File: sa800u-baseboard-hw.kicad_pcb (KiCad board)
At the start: 2 copper layers, 100 x 70 mm, 346 parts, among them IC1 TPS2378DDA, IC2 AP22652W6-7, J1 5-2337992-8, J10 1053091202, J11 WE_632723300011, J2 46756-1001, J3 WE_632723300011, J4 WE_632723300011, J5 3-84952-0, J6 F52R-1A7H1-11020, J7 MC-HVT1-S04-G, J8 WE_68715014522, J9 2908-05WB-MG, Q1 2N7000, Q2 2N7000, Q3 2N7000, Q4 2N7000, Q5 BSS84PH6327XTSA2, Q6 IRF7416TRPBF, U1 RTL8111H, U10 SA800U-WF, U11 MAX13042EEBC+T, U12 MDT580M01001, U13 AP62301WU-7, U14 AP62301WU-7, U15 AP62301WU-7, U16 LMV431IM5, U17 AP62301WU-7, U18 STUSB4500QTR, U2 LT9611, U3 TXB0104RUT, U4 TXS0102YZPR, U5 TPS25820DSST, U6 TS3USB30EDGSR, U7 TXB0104D, U8 CBTL02043ABQ,115, U9 FT2232HL-REEL, Y1 ABM8G-25.000MHZ-18-D2Y-T, Y2 ABM8G-24.000MHZ-18-D2Y-T

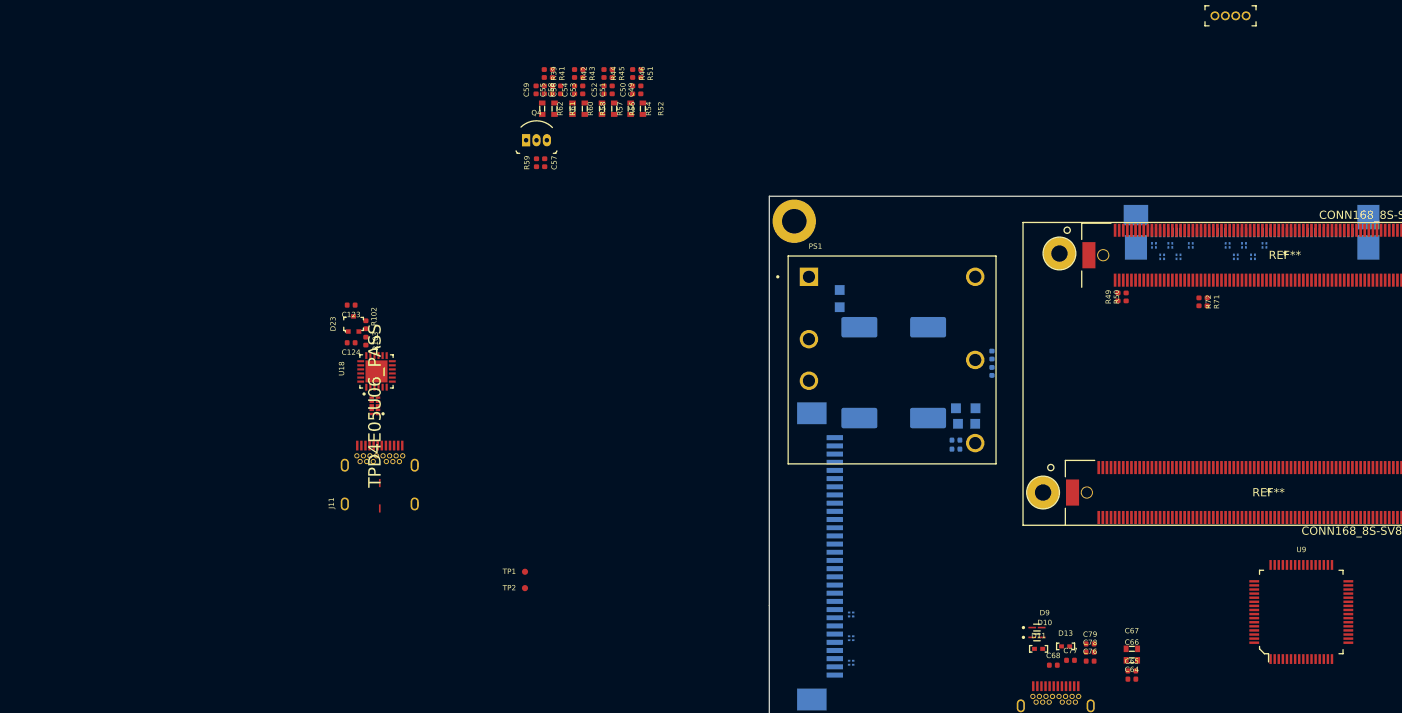
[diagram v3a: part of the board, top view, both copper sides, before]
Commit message: Import changes to PCB, group components
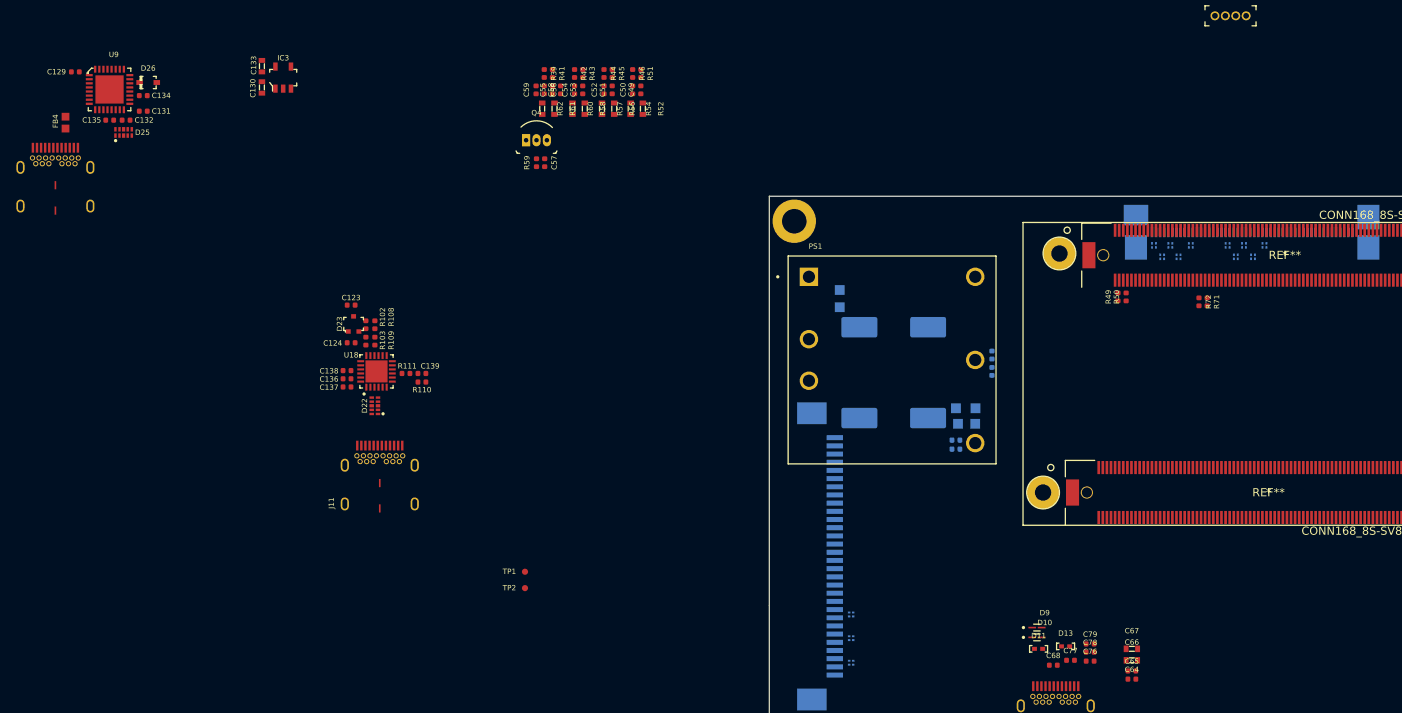
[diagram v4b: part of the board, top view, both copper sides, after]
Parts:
- added C129: C_100n_0402, sa800u-baseboard-hw-footprints:0402-cap, F.Cu at (-29.8, 66.8)
- added C130: C_2u2_0603, sa800u-baseboard-hw-footprints:0603-cap, F.Cu at (-7.00, 68.7)
- added C131: C_100n_0402, sa800u-baseboard-hw-footprints:0402-cap, F.Cu at (-21.5, 71.6)
- added C132: C_47p_0402, sa800u-baseboard-hw-footprints:0402-cap, F.Cu at (-23.6, 72.7)
- added C133: C_1u_0603, sa800u-baseboard-hw-footprints:0603-cap, F.Cu at (-7.00, 66.1)
- added C134: C_100n_0402, sa800u-baseboard-hw-footprints:0402-cap, F.Cu at (-21.5, 69.7)
- added C135: C_47p_0402, sa800u-baseboard-hw-footprints:0402-cap, F.Cu at (-25.6, 72.7)
- added C136: C_1u_0402, sa800u-baseboard-hw-footprints:0402-cap, F.Cu at (3.40, 104.3)
- added C137: C_1u_0402, sa800u-baseboard-hw-footprints:0402-cap, F.Cu at (3.40, 105.3)
- added C138: C_1u_0402, sa800u-baseboard-hw-footprints:0402-cap, F.Cu at (3.40, 103.3)
- added C139: C_100n_0402, sa800u-baseboard-hw-footprints:0402-cap, F.Cu at (12.6, 103.7)
- added D25: TPD4E05U06_PASS, sa800u-baseboard-hw-footprints:TPD4E05U06_PASS, F.Cu at (-23.9, 74.2)
- added D26: 1N4148WS, sa800u-baseboard-hw-footprints:SOD-323F, F.Cu at (-20.9, 68.1)
- added FB4: BLM18EG221SN1D, sa800u-baseboard-hw-footprints:0603, F.Cu at (-31.0, 73.0)
- added IC3: TPS7A0518PDBVT, sa800u-baseboard-hw-footprints:SOT-23-5, F.Cu at (-4.40, 67.5)
- added J12: WE_632723300011, sa800u-baseboard-hw-footprints:WE_632723300011, F.Cu at (-32.2, 81.7)
- added R108: R_100k_0402, sa800u-baseboard-hw-footprints:0402-res, F.Cu at (6.80, 97.7)
- added R109: R_22k_0402, sa800u-baseboard-hw-footprints:0402-res, F.Cu at (6.80, 99.7)
- added R110: R_100R_0402, sa800u-baseboard-hw-footprints:0402-res, F.Cu at (12.6, 104.7)
- added R111: R_1k1_0402, sa800u-baseboard-hw-footprints:0402-res, F.Cu at (10.6, 103.7)
- U9: value FT2232HL-REEL -> FT232RQ-REEL; footprint sa800u-baseboard-hw-footprints:LQFP-64_10x10mm -> sa800u-baseboard-hw-footprints:QFN-32-1EP_5x5mm
- moved U9 158.3 mm to (-25.1, 69.4)
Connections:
- U10 pad 2_135: (no net) -> DBG_RXD
- U10 pad 2_137: (no net) -> DBG_TXD
- U18 pad 16: (no net) -> Net-(R109-Pad2)
- U18 pad 21: (no net) -> Net-(C138-Pad1)
- U18 pad 22: (no net) -> GND
- U18 pad 23: (no net) -> /USB-PD/2V7
- U18 pad 24: (no net) -> /USB-PD/PD_VBUS
- U18 pad 9: (no net) -> /USB-PD/STUSB4500_DISCHARGE
- U9 pad 1: Net-(U9-Pad1) -> 1V8_DBG
- U9 pad 11: Net-(U9-Pad1) -> (no net)
- U9 pad 14: (no net) -> /USB-C_Interface /DBG_USB_D_P
- U9 pad 15: Net-(U9-Pad1) -> /USB-C_Interface /DBG_USB_D_N
- U9 pad 16: (no net) -> Net-(C131-Pad1)
- U9 pad 17: (no net) -> GND
- U9 pad 19: (no net) -> /USB-C_Interface /5V0_DBG
- U9 pad 2: (no net) -> DBG_TXD
- U9 pad 20: (no net) -> GND
- U9 pad 24: (no net) -> GND
- U9 pad 25: Net-(U9-Pad1) -> (no net)
- U9 pad 26: (no net) -> GND
- U9 pad 30: (no net) -> DBG_RXD
- U9 pad 33: (no net) -> GND
- U9 pad 4: (no net) -> GND
- U9 pad 5: Net-(U9-Pad1) -> (no net)

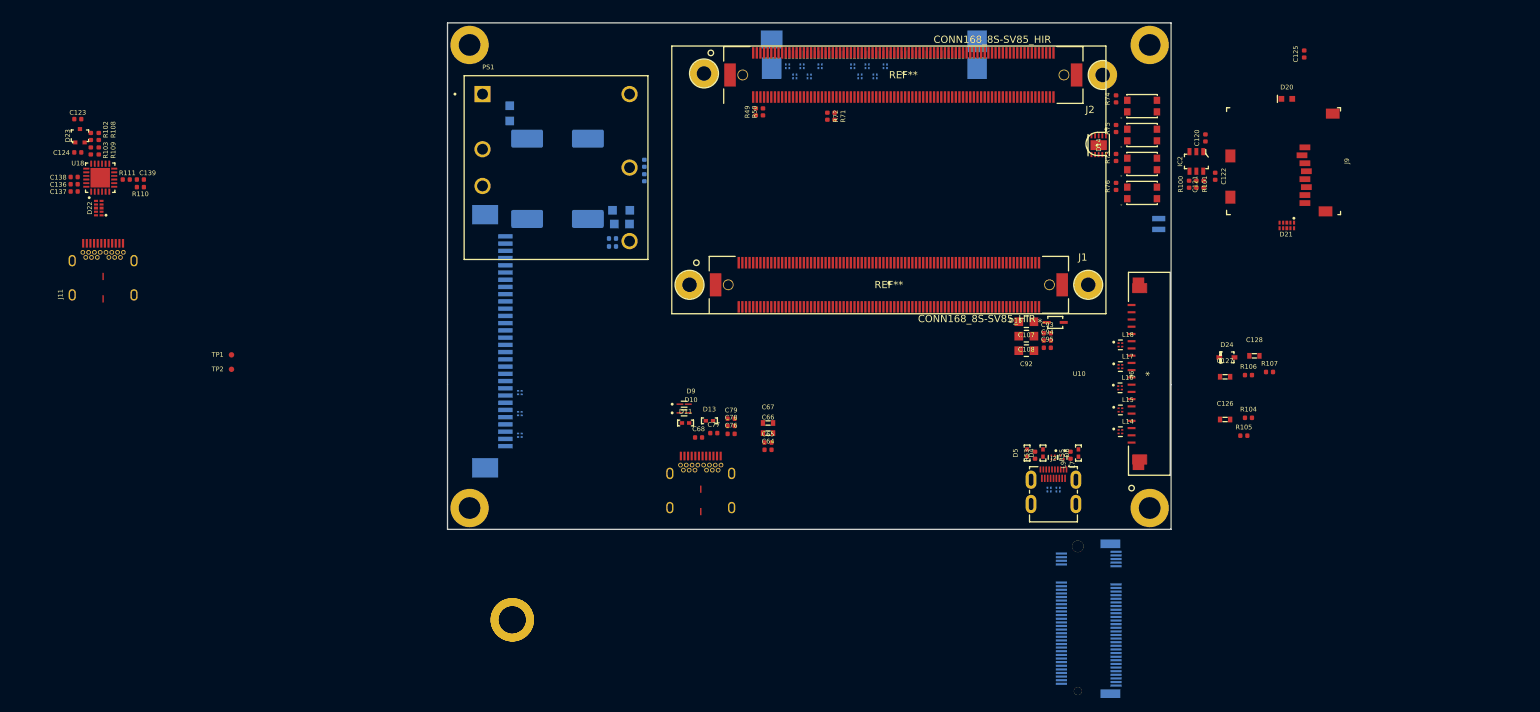
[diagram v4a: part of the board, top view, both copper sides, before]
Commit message: Import changes to PCB, group components
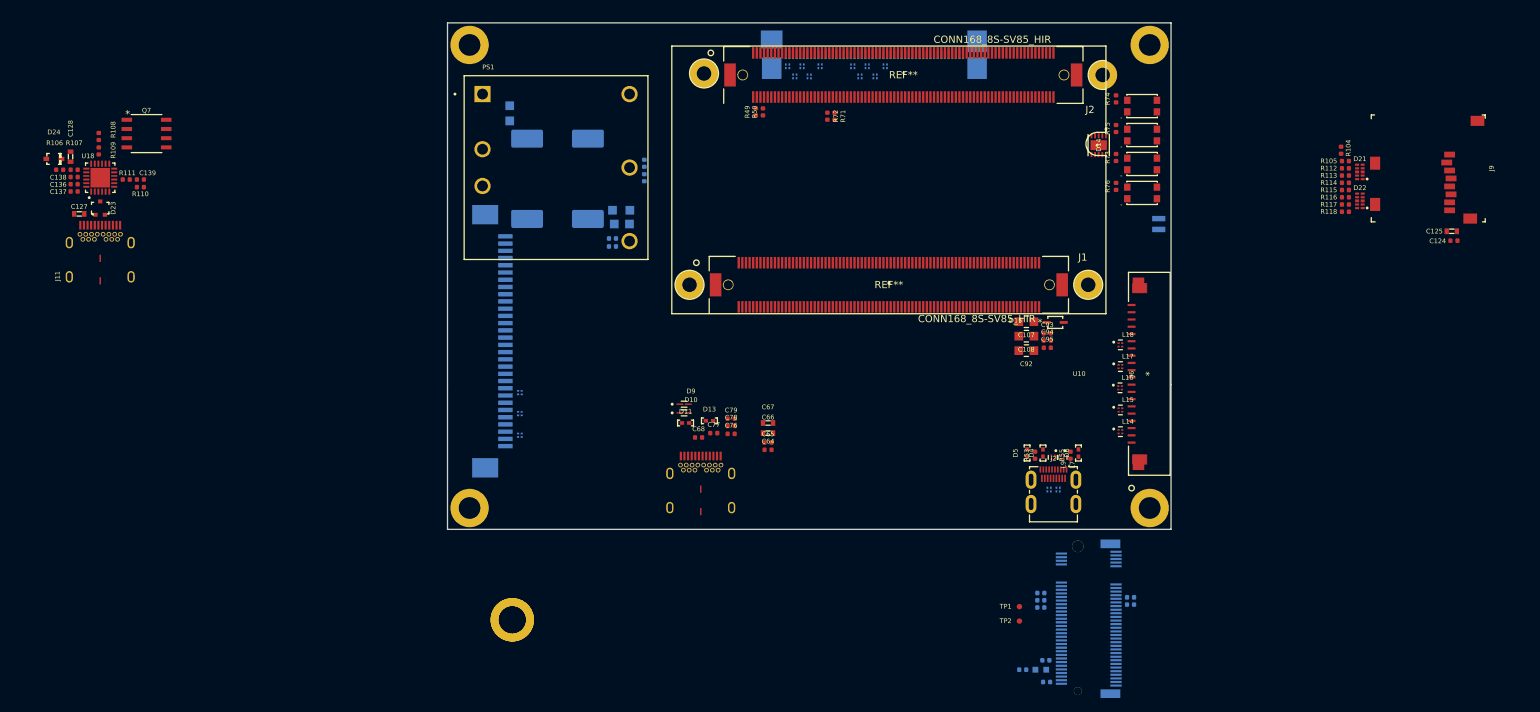
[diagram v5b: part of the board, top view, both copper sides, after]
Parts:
- removed C126: C_10u_0603, sa800u-baseboard-hw-footprints:0603-cap
- removed IC2: AP22652W6-7, sa800u-baseboard-hw-footprints:SOT-23-6
- added Q7: IRF7404TRPBF, sa800u-baseboard-hw-footprints:IRF7416TRPBF, F.Cu at (13.4, 97.3)
- added R112: R_33R_0402, antmicro-footprints:0402-res, F.Cu at (179.1, 102.1)
- added R113: R_33R_0402, antmicro-footprints:0402-res, F.Cu at (179.1, 103.1)
- added R114: R_33R_0402, antmicro-footprints:0402-res, F.Cu at (179.1, 104.1)
- added R115: R_0R_0402, antmicro-footprints:0402-res, F.Cu at (179.1, 105.1)
- added R116: R_33R_0402, antmicro-footprints:0402-res, F.Cu at (179.1, 106.1)
- added R117: R_33R_0402, antmicro-footprints:0402-res, F.Cu at (179.1, 107.1)
- added R118: R_33R_0402, antmicro-footprints:0402-res, F.Cu at (179.1, 108.1)
- C120, C121, C122, C123, D20, R100, R101, R102, R103: moved to B.Cu
- C124: value C_100n_0402 -> C_10p_0402
- C125: value C_100n_0402 -> C_2u2_0603; footprint sa800u-baseboard-hw-footprints:0402-cap -> antmicro-footprints:0603-cap
- R104: value R_10k_0402 -> R_100k_0402
- R105: value R_20k_0402 -> R_1k_0402
- moved C124 190.6 mm to (194.1, 112.1)
- moved D22 174.3 mm to (181.1, 106.6)
- moved R107 167.6 mm to (3.40, 102.3)
- moved R106 166.7 mm to (1.40, 102.3)
- moved C128 165.9 mm to (2.90, 100.5), turned to 90 degrees
- moved D24 164.4 mm to (0.60, 100.8), turned to 180 degrees
- moved C123 160.2 mm to (149.4, 162.4)
- moved C127 160.0 mm to (4.10, 108.4), turned to 180 degrees
- moved R102 148.4 mm to (134.5, 171.4), turned to 0 degrees
- moved R103 145.7 mm to (137.0, 162.8), turned to 0 degrees
- moved TP1 114.3 mm to (134.0, 162.7)
- moved TP2 114.3 mm to (134.0, 164.7)
- moved D20 85.9 mm to (137.0, 171.4), turned to 180 degrees
- moved C120 75.5 mm to (137.7, 170.1), turned to 180 degrees
- moved C121 72.1 mm to (137.8, 173.1), turned to 180 degrees
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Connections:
- C124 pad 1: GND -> /Other_Interfaces/SD_VDD_R
- C124 pad 2: 3V3 -> GND
- C125 pad 1: GND -> /Other_Interfaces/SD_VDD_R
- C125 pad 2: /Other_Interfaces/SDMCC_VDD -> GND
- D21 pad 1: SD_DATA3 -> /Other_Interfaces/SD_CMD_R
- D21 pad 2: SD_DATA2 -> /Other_Interfaces/SD_DATA3_R
- D21 pad 4: SD_DET -> /Other_Interfaces/SD_DATA2_R
- D21 pad 5: Net-(D21-Pad5) -> /Other_Interfaces/SD_DET_R
- D22 pad 1: SD_DATA1 -> /Other_Interfaces/SD_DATA1_R
- D22 pad 2: SD_DATA0 -> /Other_Interfaces/SD_DATA0_R
- D22 pad 4: SD_CLK -> /Other_Interfaces/SD_CLK_R
- D22 pad 5: SD_CMD -> /Other_Interfaces/SD_VDD_R
- J9 pad 1: SD_DATA2 -> /Other_Interfaces/SD_DATA2_R
- J9 pad 2: SD_DATA3 -> /Other_Interfaces/SD_DATA3_R
- J9 pad 3: SD_CMD -> /Other_Interfaces/SD_CMD_R
- J9 pad 4: /Other_Interfaces/SDMCC_VDD -> /Other_Interfaces/SD_VDD_R
- J9 pad 5: SD_CLK -> /Other_Interfaces/SD_CLK_R
- J9 pad 7: SD_DATA0 -> /Other_Interfaces/SD_DATA0_R
- J9 pad 8: SD_DATA1 -> /Other_Interfaces/SD_DATA1_R
- R104 pad 1: 3V3 -> 1V8
- R104 pad 2: /Other_Interfaces/SDMCC_VDD_FAULT# -> SD_DET
- R105 pad 1: /Other_Interfaces/SDMCC_VDD_ILIM -> SD_DET
- R105 pad 2: GND -> /Other_Interfaces/SD_DET_R

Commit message: Loclib
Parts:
- C125: footprint antmicro-footprints:0603-cap -> sa800u-baseboard-hw-footprints:0603-cap
- R112, R113, R114, R115, R116, R117, R118: footprint antmicro-footprints:0402-res -> sa800u-baseboard-hw-footprints:0402-res
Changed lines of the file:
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@@
     (add_net WCD_CLK)
   )
-  (module antmicro-footprints:0402-res (layer F.Cu)
+  (module sa800u-baseboard-hw-footprints:0402-res (layer F.Cu)
     (at 179.1 108.1)
     (descr "Resistor SMD 0402 (1005 Metric), square (rectangular) end terminal, IPC_7351 nominal, (Body size source: http://www.tortai-tech.com/upload/download/2011102023233369053.pdf), generated with kicad-footprint-generator")
@@
     (pad 1 smd roundrect (at -0.485 0) (size 0.59 0.64) (layers F.Cu F.Paste F.Mask) (roundrect_rratio 0.25)
       (net 313 SD_DATA1))
-    (model ${ANT3DMDL}/0402-res.step
-      (offset (xyz 0 0 -0.01))
-      (scale (xyz 1 1 1))
-      (rotate (xyz 0 0 0))
-    )
-  )
-  (module antmicro-footprints:0402-res (layer F.Cu)
+    (model ${KIPRJMOD}/lib/3d-models/0402-res.step
+      (offset (xyz 0 0 -0.01))
+      (scale (xyz 1 1 1))
+      (rotate (xyz 0 0 0))
+    )
+  )
+  (module sa800u-baseboard-hw-footprints:0402-res (layer F.Cu)
     (at 179.1 107.1)
     (descr "Resistor SMD 0402 (1005 Metric), square (rectangular) end terminal, IPC_7351 nominal, (Body size source: http://www.tortai-tech.com/upload/download/2011102023233369053.pdf), generated with kicad-footprint-generator")
@@
     (pad 1 smd roundrect (at -0.485 0) (size 0.59 0.64) (layers F.Cu F.Paste F.Mask) (roundrect_rratio 0.25)
       (net 314 SD_DATA0))
-    (model ${ANT3DMDL}/0402-res.step
-      (offset (xyz 0 0 -0.01))
-      (scale (xyz 1 1 1))
-      (rotate (xyz 0 0 0))
-    )
-  )
-  (module antmicro-footprints:0402-res (layer F.Cu)
+    (model ${KIPRJMOD}/lib/3d-models/0402-res.step
+      (offset (xyz 0 0 -0.01))
+      (scale (xyz 1 1 1))
+      (rotate (xyz 0 0 0))
+    )
+  )
+  (module sa800u-baseboard-hw-footprints:0402-res (layer F.Cu)
     (at 179.1 106.1)
     (descr "Resistor SMD 0402 (1005 Metric), square (rectangular) end terminal, IPC_7351 nominal, (Body size source: http://www.tortai-tech.com/upload/download/2011102023233369053.pdf), generated with kicad-footprint-generator")
@@
     (pad 1 smd roundrect (at -0.485 0) (size 0.59 0.64) (layers F.Cu F.Paste F.Mask) (roundrect_rratio 0.25)
       (net 312 SD_CLK))
-    (model ${ANT3DMDL}/0402-res.step
-      (offset (xyz 0 0 -0.01))
-      (scale (xyz 1 1 1))
-      (rotate (xyz 0 0 0))
-    )
-  )
-  (module antmicro-footprints:0402-res (layer F.Cu)
+    (model ${KIPRJMOD}/lib/3d-models/0402-res.step
+      (offset (xyz 0 0 -0.01))
+      (scale (xyz 1 1 1))
+      (rotate (xyz 0 0 0))
+    )
+  )
+  (module sa800u-baseboard-hw-footprints:0402-res (layer F.Cu)
     (at 179.1 105.1)
     (descr "Resistor SMD 0402 (1005 Metric), square (rectangular) end terminal, IPC_7351 nominal, (Body size source: http://www.tortai-tech.com/upload/download/2011102023233369053.pdf), generated with kicad-footprint-generator")
@@
     (pad 1 smd roundrect (at -0.485 0) (size 0.59 0.64) (layers F.Cu F.Paste F.Mask) (roundrect_rratio 0.25)
       (net 299 SD_LDO21A))
-    (model ${ANT3DMDL}/0402-res.step
-      (offset (xyz 0 0 -0.01))
-      (scale (xyz 1 1 1))
-      (rotate (xyz 0 0 0))
-    )
-  )
-  (module antmicro-footprints:0402-res (layer F.Cu)
+    (model ${KIPRJMOD}/lib/3d-models/0402-res.step
+      (offset (xyz 0 0 -0.01))
+      (scale (xyz 1 1 1))
+      (rotate (xyz 0 0 0))
+    )
+  )
+  (module sa800u-baseboard-hw-footprints:0402-res (layer F.Cu)
     (at 179.1 104.1)
     (descr "Resistor SMD 0402 (1005 Metric), square (rectangular) end terminal, IPC_7351 nominal, (Body size source: http://www.tortai-tech.com/upload/download/2011102023233369053.pdf), generated with kicad-footprint-generator")
@@
     (pad 1 smd roundrect (at -0.485 0) (size 0.59 0.64) (layers F.Cu F.Paste F.Mask) (roundrect_rratio 0.25)
       (net 311 SD_CMD))
-    (model ${ANT3DMDL}/0402-res.step
-      (offset (xyz 0 0 -0.01))
-      (scale (xyz 1 1 1))
-      (rotate (xyz 0 0 0))
-    )
-  )
-  (module antmicro-footprints:0402-res (layer F.Cu)
+    (model ${KIPRJMOD}/lib/3d-models/0402-res.step
+      (offset (xyz 0 0 -0.01))
+      (scale (xyz 1 1 1))
+      (rotate (xyz 0 0 0))
+    )
+  )
+  (module sa800u-baseboard-hw-footprints:0402-res (layer F.Cu)
     (at 179.1 103.1)
     (descr "Resistor SMD 0402 (1005 Metric), square (rectangular) end terminal, IPC_7351 nominal, (Body size source: http://www.tortai-tech.com/upload/download/2011102023233369053.pdf), generated with kicad-footprint-generator")
@@
     (pad 1 smd roundrect (at -0.485 0) (size 0.59 0.64) (layers F.Cu F.Paste F.Mask) (roundrect_rratio 0.25)
       (net 309 SD_DATA3))
-    (model ${ANT3DMDL}/0402-res.step
-      (offset (xyz 0 0 -0.01))
-      (scale (xyz 1 1 1))
-      (rotate (xyz 0 0 0))
-    )
-  )
-  (module antmicro-footprints:0402-res (layer F.Cu)
+    (model ${KIPRJMOD}/lib/3d-models/0402-res.step
+      (offset (xyz 0 0 -0.01))
+      (scale (xyz 1 1 1))
+      (rotate (xyz 0 0 0))
+    )
+  )
+  (module sa800u-baseboard-hw-footprints:0402-res (layer F.Cu)
     (at 179.1 102.1)
     (descr "Resistor SMD 0402 (1005 Metric), square (rectangular) end terminal, IPC_7351 nominal, (Body size source: http://www.tortai-tech.com/upload/download/2011102023233369053.pdf), generated with kicad-footprint-generator")
@@
     (pad 1 smd roundrect (at -0.485 0) (size 0.59 0.64) (layers F.Cu F.Paste F.Mask) (roundrect_rratio 0.25)
       (net 310 SD_DATA2))
-    (model ${ANT3DMDL}/0402-res.step
+    (model ${KIPRJMOD}/lib/3d-models/0402-res.step
       (offset (xyz 0 0 -0.01))
       (scale (xyz 1 1 1))
@@
     )
   )
-  (module antmicro-footprints:0603-cap (layer F.Cu)
+  (module sa800u-baseboard-hw-footprints:0603-cap (layer F.Cu)
     (at 193.8 110.8 180)
     (attr smd)
@@
     (pad 2 smd rect (at 0.7 0 180) (size 0.6 0.8) (layers F.Cu F.Paste F.Mask)
       (net 1 GND))
-    (model ${ANT3DMDL}/0603-cap.step
+    (model ${KIPRJMOD}/lib/3d-models/0603-cap.step
       (offset (xyz 0 -0.45 0.42))
       (scale (xyz 1 1 1))
